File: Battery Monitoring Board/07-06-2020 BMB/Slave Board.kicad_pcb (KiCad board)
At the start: 2 copper layers, 438 x 77.5 mm, 149 parts, among them IC1 LTC6820IMS#PBF, IC2 LTC6804-2, J1 Conn_01x02, J10 Conn_01x02, J11 Conn_01x02, J12 Conn_01x02, J13 Conn_01x06, J14 Conn_01x01, J15 Conn_01x01, J16 Conn_01x01, J17 Conn_01x01, J18 Conn_01x01, J19 Conn_01x01, J2 Conn_01x02, J20 Conn_01x01, J21 Conn_01x01, J22 Conn_01x01, J23 Conn_01x01, J24 Conn_01x01, J25 Conn_01x01, J26 Conn_01x01, J3 Conn_01x02, J4 Conn_01x02, J5 Conn_01x02, J6 Conn_01x02, J7 Conn_01x02, J8 Conn_01x02, J9 Conn_01x02, Q1 Q_NPN_BCE, Q10 Q_PMOS_GSD, Q11 Q_PMOS_GSD, Q12 Q_PMOS_GSD, Q13 Q_PMOS_GSD, Q2 Q_PMOS_GSD, Q3 Q_PMOS_GSD, Q4 Q_PMOS_GSD, Q5 Q_PMOS_GSD, Q6 Q_PMOS_GSD, Q7 Q_PMOS_GSD, Q8 Q_PMOS_GSD, Q9 Q_PMOS_GSD, T1 PE-68386NL, U1 MCP2551_CANmodule, U2 MCP2551-I-SN, U3 OKI-78SR-3.3_1.5-W36-C, U4 ISO1050DUB, U5 TMR_1-1212, U6 ARDUINO_MICRO_SHIELD

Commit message: Blind mate connector added to BMB
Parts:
- added J27: Conn_01x04, Connector_Molex:Molex_KK-254_AE-6410-04A_1x04_P2.54mm_Vertical, F.Cu at (92.8, 180.2)
- J13: footprint Connector_Molex:Molex_Micro-Fit_3.0_43650-0600_1x06_P3.00mm_Horizontal -> 44764-0802:447640802
- moved J13 13.0 mm to (79.9, 184.1), turned to 270 degrees
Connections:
- J13 pad 2: GND -> +12V
- J13 pad 3: +12V -> CANH
- J13 pad 4: CANH -> CANL
- J13 pad 5: Net-(J13-Pad5) -> GND
- J13 pad 6: CANL -> DCDC+
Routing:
- net CANL: track 42.0 -> 22.1 mm
- net PWM_Fans: track 0.00 -> 15.2 mm, vias 0 -> 1
- net Sens_Fans: track 0.00 -> 14.5 mm, vias 0 -> 1
- net DCDC+: track 0.00 -> 14.2 mm, vias 0 -> 2
- net CANH: track 34.8 -> 25.9 mm
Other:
- outline, holes or cut-outs redrawn

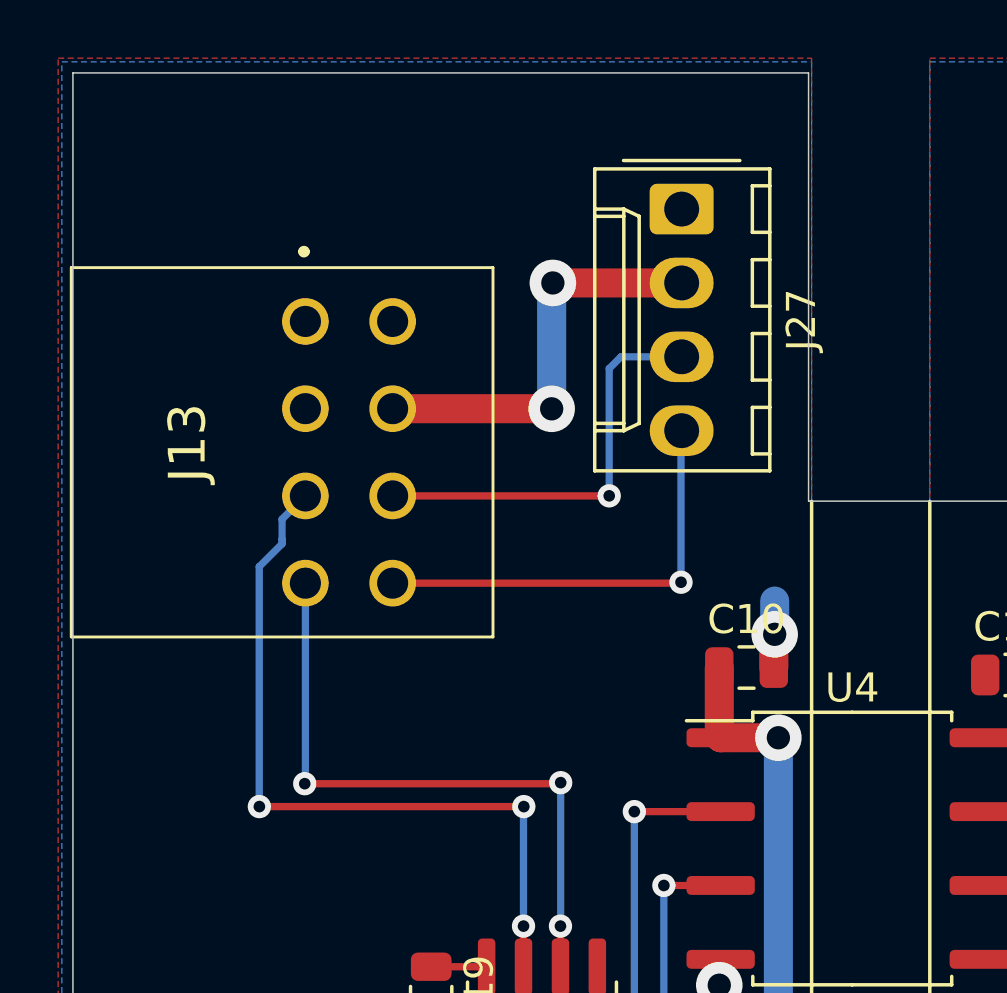
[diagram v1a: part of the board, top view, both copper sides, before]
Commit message: BMB wired BMI connector
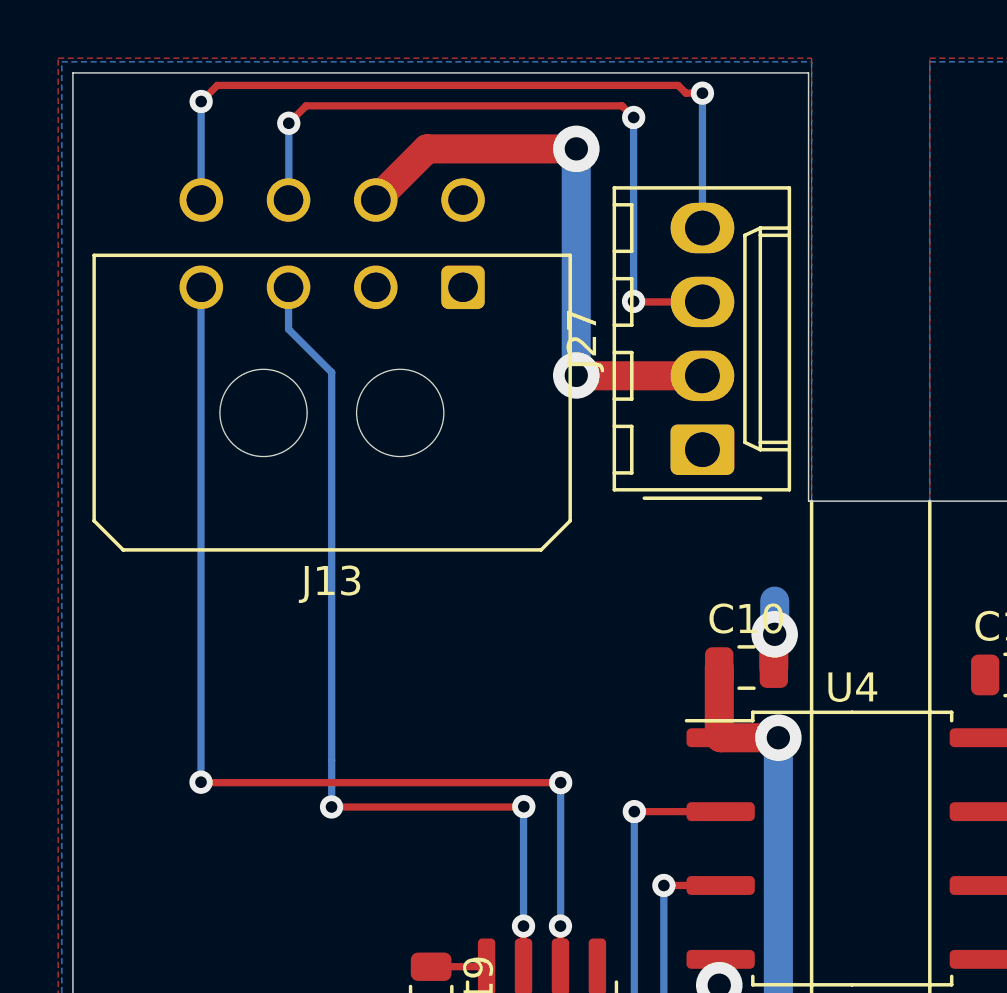
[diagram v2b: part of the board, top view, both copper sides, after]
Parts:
- J13: value Conn_01x06 -> Conn_01x08; footprint 44764-0802:447640802 -> Connector_Molex:Molex_Micro-Fit_3.0_43045-0800_2x04_P3.00mm_Horizontal
- moved J27 8.30 mm to (93.5, 188.5), turned to 90 degrees
- moved J13 5.55 mm to (85.3, 182.9), turned to 180 degrees
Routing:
- net CANL: track 22.1 -> 35.8 mm
- net PWM_Fans: track 15.2 -> 25.6 mm, vias 1 -> 2
- net Sens_Fans: track 14.5 -> 23.6 mm, vias 1 -> 3
- net DCDC+: track 14.2 -> 19.8 mm
- net CANH: track 25.9 -> 30.6 mm
